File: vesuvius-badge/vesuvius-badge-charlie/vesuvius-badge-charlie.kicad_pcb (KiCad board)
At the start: 2 copper layers, 161.6 x 89 mm, 164 parts, among them J1 Conn_01x07, J2 Conn_01x02, U1 IS31FL3731-QF, U2 Pico

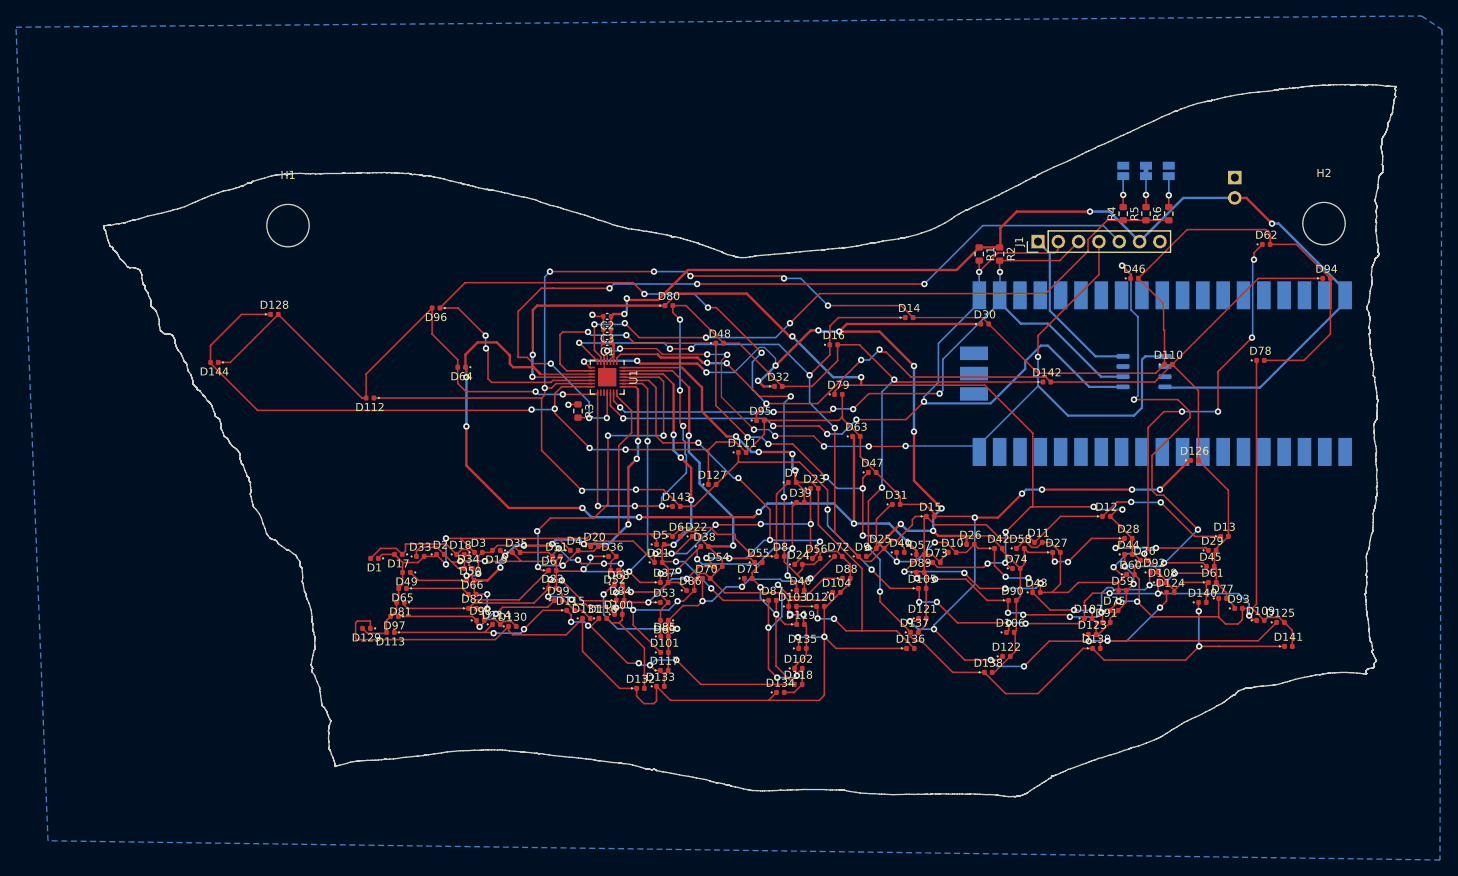
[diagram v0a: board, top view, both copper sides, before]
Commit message: redo pcb after led footprint change
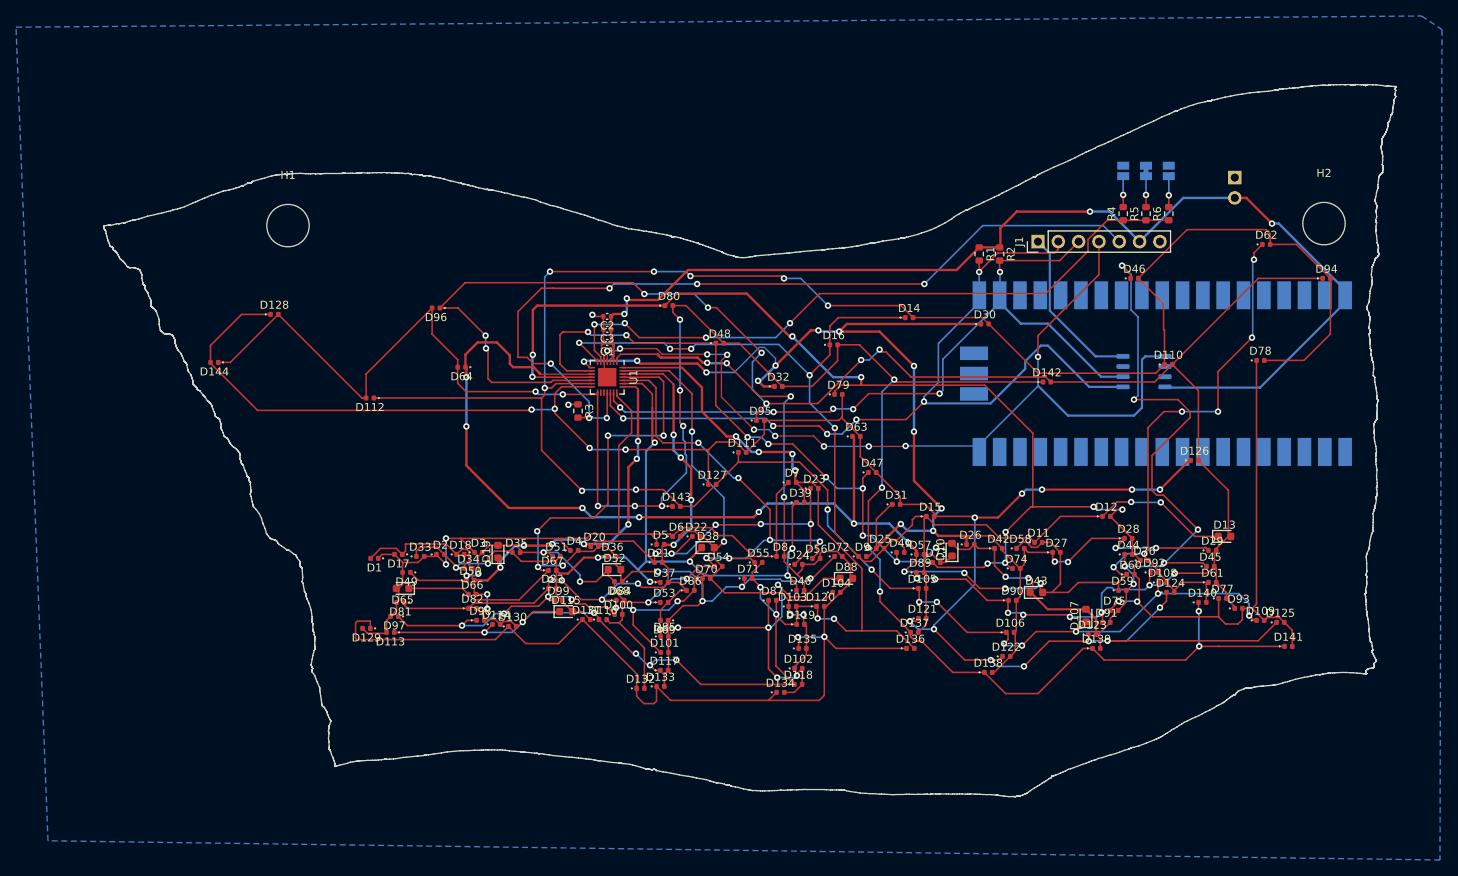
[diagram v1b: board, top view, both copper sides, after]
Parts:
- D10, D107, D115, D13, D19, D38, D43, D52, D65, D88: footprint LED_SMD:LED_0402_1005Metric -> LED_SMD:LED_0603_1608Metric
- moved D115 0.58 mm to (156.2, 114.0)
- moved D38 0.46 mm to (174.0, 106.0)
- moved D107 0.45 mm to (221.2, 114.5), turned to 90 degrees
- moved D10 0.35 mm to (204.5, 106.2), turned to 90 degrees
- moved D68 0.35 mm to (162.8, 110.2), turned to 180 degrees
- moved D19 0.25 mm to (147.8, 106.5), turned to 90 degrees
- moved D116 0.15 mm to (160.8, 115.0)
- moved D131 0.15 mm to (158.8, 115.0)
- moved D52 0.10 mm to (162.3, 108.8), turned to 0 degrees
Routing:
- net CA5: track 131.9 -> 128.7 mm, vias 10 -> 9
- net CB7: track 306.5 -> 309.4 mm
- net CA8: track 161.0 -> 163.7 mm, vias 15 -> 14
- net CA3: track 113.8 -> 111.4 mm, vias 11 -> 8
- net CA7: track 126.8 -> 125.3 mm
- net CA9: track 170.6 -> 169.7 mm
- net CB3: track 187.1 -> 186.3 mm, vias 19 -> 17
- net CA6: track 132.4 -> 133.2 mm
- net CA4: track 121.8 -> 122.4 mm, vias 14 -> 12
- net CA2: track 122.3 -> 122.7 mm, vias 15 -> 14

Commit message: finished functional parts
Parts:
- added JP4: SolderJumper_2_Open, Jumper:SolderJumper-2_P1.3mm_Open_Pad1.0x1.5mm, B.Cu at (244.5, 59.2)
- J1: value Conn_01x07 -> Conn_01x06; footprint Connector_PinHeader_2.54mm:PinHeader_1x07_P2.54mm_Vertical -> Connector_PinHeader_2.54mm:PinHeader_1x06_P2.54mm_Vertical
- moved J2 2.27 mm to (239.8, 62.0), turned to 0 degrees
- renumbered 11 to 1111
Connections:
- J2 pad 2: VCC -> +BATT
- U2 pad 36: unconnected-(U2-Pad36) -> VCC
- U2 pad 39: VCC -> +BATT
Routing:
- net +BATT: track 0.00 -> 27.0 mm
- net VCC: vias 4 -> 3

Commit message: final files and gerbers as submitted to production
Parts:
- added F1: Fuse_Small, Fuse:Fuse_0402_1005Metric, F.Cu at (244.0, 55.2)
- C3: value 0.1uF -> 100nF
- D1, D100, D101, D102, D103, D104, D105, D106, D108, D109, D11, D110, D111, D112, D113, D114, D116, D117, D118, D119, D12, D120, D121, D122, D123, D124, D125, D126, D127, D129, D130, D131, D132, D133, D134, D135, D136, D137, D138, D139, D140, D141, D143, D144, D15, D17, D18, D2, D20, D21, D22, D24, D25, D26, D27, D28, D29, D3, D31, D33, D34, D35, D36, D37, D4, D40, D41, D42, D44, D45, D47, D49, D5, D50, D51, D53, D54, D55, D56, D57, D58, D59, D6, D60, D61, D62, D63, D64, D66, D67, D68, D69, D70, D71, D72, D73, D74, D75, D76, D77, D79, D8, D81, D82, D83, D84, D85, D86, D87, D89, D9, D90, D91, D92, D93, D94, D95, D96, D97, D98, D99: value LED -> LED white
- D10, D107, D115, D13, D19, D38, D43, D52, D65, D88: value LED -> LED purple
- D128, D30, D39, D46, D78: value LED -> LED orange
- D14, D142, D16, D23, D32, D48, D7, D80: value LED -> LED red
- J1: value Conn_01x06 -> Conn_01x05; footprint Connector_PinHeader_2.54mm:PinHeader_1x06_P2.54mm_Vertical -> Connector_PinHeader_2.54mm:PinHeader_1x05_P2.54mm_Vertical; moved to B.Cu
- J2: value Conn_01x02 -> Conn_01x03; footprint Connector_PinHeader_2.54mm:PinHeader_1x02_P2.54mm_Vertical -> Connector_PinHeader_2.54mm:PinHeader_1x03_P2.54mm_Vertical
- R1, R2: value 10k -> 4k7
- moved D144 11.0 mm to (121.8, 77.2)
- moved D128 10.5 mm to (127.5, 69.8)
- moved H1 8.49 mm to (115.2, 60.0)
- moved H2 6.04 mm to (253.5, 60.0)
- moved J2 2.50 mm to (239.8, 64.5)
- moved J1 2.50 mm to (217.8, 67.8), turned to -90 degrees
- renumbered 1111 to U3
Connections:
- J1 pad 1: CH32V003_SWIO -> MCU_SDA
- J1 pad 2: MCU_SDA -> MCU_SCL
- J1 pad 3: MCU_SCL -> MCU_INTB
- J1 pad 4: MCU_INTB -> I2C-AD
- J1 pad 5: I2C-AD -> VCC
- J2 pad 1: GND -> CH32V003_SWIO
- J2 pad 2: +BATT -> GND
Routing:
- net CH32V003_SWIO: track 20.8 -> 28.5 mm
- net Net-(J2-Pad3): track 0.00 -> 6.80 mm
- net +BATT: track 27.0 -> 25.4 mm, vias 0 -> 1
- net CB9: track 269.7 -> 268.4 mm
- net VCC: track 143.5 -> 144.3 mm
- net CB3: track 186.3 -> 185.5 mm
- net CB8: track 247.9 -> 248.7 mm, vias 16 -> 15
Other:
- board size 161.6 x 89 mm -> 162.5 x 85.5 mm
- board text added: "AD"
- board text added: "Batt"
- board text added: "GND"
- board text added: "INTB"
- board text added: "JLCJLCJLCJLC"
- board text added: "SCL"
- board text added: "SDA"
- board text added: "SWIO"
- board text added: "VCC"
- board text added: "Vesuvius Badge v1 by Johannes Rudolph https://github.com/jrudolph/vesuvius-badge"
